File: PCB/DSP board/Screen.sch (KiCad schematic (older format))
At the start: 20 parts, among them J701 Conn_01x40_Female, J702 Conn_01x06_Female

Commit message: Schematic updates + PCB placement
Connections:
- net I2C1_SCL: now also RN709.2 (R2.1); no longer RN709.3 (R3.1)
- net I2C1_SDA: now also RN709.3 (R3.1); no longer RN709.4 (R4.1)
- net LCD_B0: now also RN704.1 (R1.1); no longer RN704.4 (R4.1)
- net LCD_B2: now also RN704.2 (R2.1); no longer RN704.3 (R3.1)
- net LCD_B4: now also RN704.3 (R3.1); no longer RN704.2 (R2.1)
- net LCD_B6: now also RN704.4 (R4.1); no longer RN704.1 (R1.1)
- net LCD_G0: now also RN706.1 (R1.1); no longer RN706.4 (R4.1)
- net LCD_G2: now also RN706.2 (R2.1); no longer RN706.3 (R3.1)
- net LCD_G4: now also RN706.3 (R3.1); no longer RN706.2 (R2.1)
- net LCD_G6: now also RN706.4 (R4.1); no longer RN706.1 (R1.1)
- net LCD_R0: now also RN708.1 (R1.1); no longer RN708.4 (R4.1)
- net LCD_R2: now also RN708.2 (R2.1); no longer RN708.3 (R3.1)
- net LCD_R4: now also RN708.3 (R3.1); no longer RN708.2 (R2.1)
- net LCD_R6: now also RN708.4 (R4.1); no longer RN708.1 (R1.1)
- net LCD_VSYNC: now also RN702.1 (R1.1); no longer RN702.4 (R4.1)
- net TFT_B0: now also RN704.8 (R1.2); no longer RN704.5 (R4.2)
- net TFT_B2: now also RN704.7 (R2.2); no longer RN704.6 (R3.2)
- net TFT_B4: now also RN704.6 (R3.2); no longer RN704.7 (R2.2)
- net TFT_B6: now also RN704.5 (R4.2); no longer RN704.8 (R1.2)
- net TFT_G0: now also RN706.8 (R1.2); no longer RN706.5 (R4.2)
- net TFT_G2: now also RN706.7 (R2.2); no longer RN706.6 (R3.2)
- net TFT_G4: now also RN706.6 (R3.2); no longer RN706.7 (R2.2)
- net TFT_G6: now also RN706.5 (R4.2); no longer RN706.8 (R1.2)
- net TFT_NINT: now also RN709.8 (R1.2); no longer RN709.7 (R2.2)
- net TFT_NRESET: now also RN709.5 (R4.2); no longer RN709.8 (R1.2)
- net TFT_R0: now also RN708.8 (R1.2); no longer RN708.5 (R4.2)
- net TFT_R2: now also RN708.7 (R2.2); no longer RN708.6 (R3.2)
- net TFT_R4: now also RN708.6 (R3.2); no longer RN708.7 (R2.2)
- net TFT_R6: now also RN708.5 (R4.2); no longer RN708.8 (R1.2)
- net TFT_SCL: now also RN709.7 (R2.2); no longer RN709.5 (R4.2)
- net TFT_VSD: now also RN702.8 (R1.2); no longer RN702.5 (R4.2)
- net TOUCH_NINT: now also RN709.1 (R1.1); no longer RN709.2 (R2.1)
- net TOUCH_NRESET: now also RN709.4 (R4.1); no longer RN709.1 (R1.1)
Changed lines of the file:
@@
 	0    1    1    0
 $EndComp
+Text GLabel 1575 7100 0    60   Input ~ 0
+LCD_R0
+Text GLabel 1575 7200 0    60   Input ~ 0
+LCD_R2
+Text GLabel 1575 7300 0    60   Input ~ 0
+LCD_R4
 Text GLabel 1575 7400 0    60   Input ~ 0
-LCD_R0
-Text GLabel 1575 7300 0    60   Input ~ 0
-LCD_R2
-Text GLabel 1575 7200 0    60   Input ~ 0
-LCD_R4
-Text GLabel 1575 7100 0    60   Input ~ 0
 LCD_R6
 Text GLabel 1575 6625 0    60   Input ~ 0
@@
 Text GLabel 1575 6325 0    60   Input ~ 0
 LCD_R7
+Text GLabel 1575 5550 0    60   Input ~ 0
+LCD_G0
+Text GLabel 1575 5650 0    60   Input ~ 0
+LCD_G2
+Text GLabel 1575 5750 0    60   Input ~ 0
+LCD_G4
 Text GLabel 1575 5850 0    60   Input ~ 0
-LCD_G0
-Text GLabel 1575 5750 0    60   Input ~ 0
-LCD_G2
-Text GLabel 1575 5650 0    60   Input ~ 0
-LCD_G4
-Text GLabel 1575 5550 0    60   Input ~ 0
 LCD_G6
 Text GLabel 1575 5050 0    60   Input ~ 0
@@
 Text GLabel 1575 4750 0    60   Input ~ 0
 LCD_G7
+Text GLabel 1575 3975 0    60   Input ~ 0
+LCD_B0
+Text GLabel 1575 4075 0    60   Input ~ 0
+LCD_B2
+Text GLabel 1575 4175 0    60   Input ~ 0
+LCD_B4
 Text GLabel 1575 4275 0    60   Input ~ 0
-LCD_B0
-Text GLabel 1575 4175 0    60   Input ~ 0
-LCD_B2
-Text GLabel 1575 4075 0    60   Input ~ 0
-LCD_B4
-Text GLabel 1575 3975 0    60   Input ~ 0
 LCD_B6
 Text GLabel 1575 3500 0    60   Input ~ 0
@@
 	0    1    1    0
 $EndComp
-Text GLabel 1575 2725 0    60   Input ~ 0
+Text GLabel 1575 2425 0    60   Input ~ 0
 LCD_VSYNC
 Text GLabel 1550 1975 0    60   Input ~ 0
@@
 	1550 1975 1700 1975
 Wire Wire Line
-	1575 2725 1700 2725
+	1575 2425 1700 2425
 Wire Wire Line
 	1575 3200 1700 3200
@@
 Text GLabel 2200 1975 2    60   Output ~ 0
 TFT_CLKIN
-Text GLabel 2200 2725 2    60   Output ~ 0
+Text GLabel 2200 2425 2    60   Output ~ 0
 TFT_VSD
 Text GLabel 2200 3200 2    60   Output ~ 0
@@
 Text GLabel 2200 3500 2    60   Output ~ 0
 TFT_B1
+Text GLabel 2200 4275 2    60   Output ~ 0
+TFT_B6
+Text GLabel 2200 4175 2    60   Output ~ 0
+TFT_B4
+Text GLabel 2200 4075 2    60   Output ~ 0
+TFT_B2
 Text GLabel 2200 3975 2    60   Output ~ 0
-TFT_B6
-Text GLabel 2200 4075 2    60   Output ~ 0
-TFT_B4
-Text GLabel 2200 4175 2    60   Output ~ 0
-TFT_B2
-Text GLabel 2200 4275 2    60   Output ~ 0
 TFT_B0
 Text GLabel 2200 4750 2    60   Output ~ 0
@@
 Text GLabel 2200 5050 2    60   Output ~ 0
 TFT_G1
+Text GLabel 2200 5850 2    60   Output ~ 0
+TFT_G6
+Text GLabel 2200 5750 2    60   Output ~ 0
+TFT_G4
+Text GLabel 2200 5650 2    60   Output ~ 0
+TFT_G2
 Text GLabel 2200 5550 2    60   Output ~ 0
-TFT_G6
-Text GLabel 2200 5650 2    60   Output ~ 0
-TFT_G4
-Text GLabel 2200 5750 2    60   Output ~ 0
-TFT_G2
-Text GLabel 2200 5850 2    60   Output ~ 0
 TFT_G0
 Text GLabel 2200 6325 2    60   Output ~ 0
@@
 Text GLabel 2200 6625 2    60   Output ~ 0
 TFT_R1
+Text GLabel 2200 7400 2    60   Output ~ 0
+TFT_R6
+Text GLabel 2200 7300 2    60   Output ~ 0
+TFT_R4
+Text GLabel 2200 7200 2    60   Output ~ 0
+TFT_R2
 Text GLabel 2200 7100 2    60   Output ~ 0
-TFT_R6
-Text GLabel 2200 7200 2    60   Output ~ 0
-TFT_R4
-Text GLabel 2200 7300 2    60   Output ~ 0
-TFT_R2
-Text GLabel 2200 7400 2    60   Output ~ 0
 TFT_R0
 Wire Wire Line
@@
 	2100 1975 2200 1975
 Wire Wire Line
-	2100 2725 2200 2725
+	2100 2425 2200 2425
 Wire Wire Line
 	2100 3200 2200 3200
@@
 	0    1    1    0
 $EndComp
-Text GLabel 8100 1650 2    60   Output ~ 0
+Text GLabel 8100 1950 2    60   Output ~ 0
 TFT_NRESET
-Text GLabel 8100 1750 2    60   Input ~ 0
+Text GLabel 8100 1650 2    60   Input ~ 0
 TFT_NINT
 Text GLabel 8100 1850 2    60   BiDi ~ 0
 TFT_SDA
-Text GLabel 8100 1950 2    60   BiDi ~ 0
+Text GLabel 8100 1750 2    60   BiDi ~ 0
 TFT_SCL
 Wire Wire Line
@@
 Wire Wire Line
 	8000 1650 8100 1650
+Text GLabel 7500 1750 0    60   BiDi ~ 0
+I2C1_SCL
 Text GLabel 7500 1850 0    60   BiDi ~ 0
-I2C1_SCL
-Text GLabel 7500 1950 0    60   BiDi ~ 0
 I2C1_SDA
-Text GLabel 7500 1650 0    60   Input ~ 0
+Text GLabel 7500 1950 0    60   Input ~ 0
 TOUCH_NRESET
-Text GLabel 7500 1750 0    60   Output ~ 0
+Text GLabel 7500 1650 0    60   Output ~ 0
 TOUCH_NINT
 Wire Wire Line
@@
 NoConn ~ 1700 1675
 NoConn ~ 2100 1675
-NoConn ~ 1700 2425
-NoConn ~ 2100 2425
-NoConn ~ 2100 2525
-NoConn ~ 2100 2625
-NoConn ~ 1700 2625
-NoConn ~ 1700 2525
 NoConn ~ 3900 2025
 NoConn ~ 3900 3350
 NoConn ~ 3900 3450
 NoConn ~ 3900 3550
+NoConn ~ 1700 2525
+NoConn ~ 1700 2625
+NoConn ~ 1700 2725
+NoConn ~ 2100 2525
+NoConn ~ 2100 2625
+NoConn ~ 2100 2725
 $EndSCHEMATC

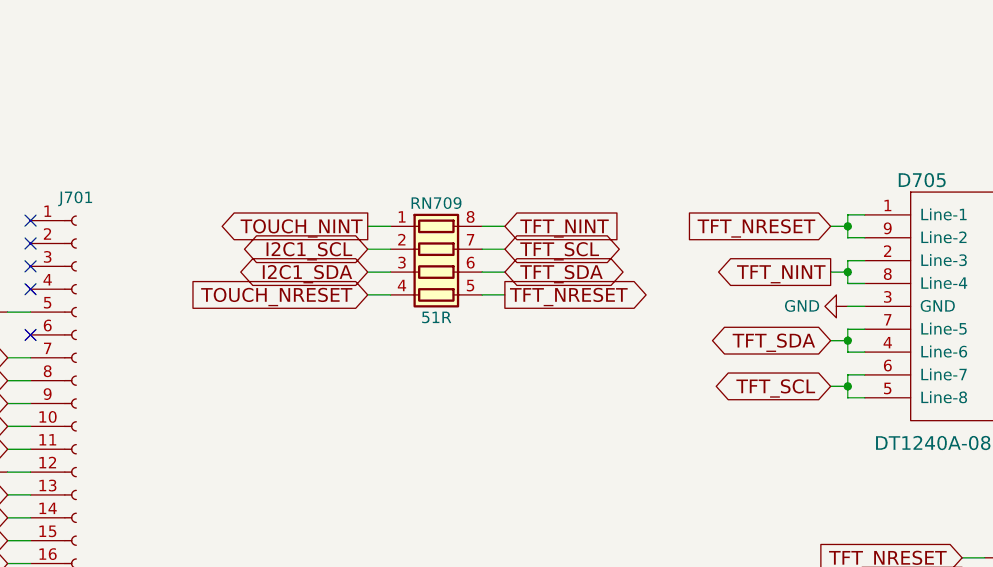
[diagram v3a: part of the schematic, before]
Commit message: Component Placement - RN
All components placed except for RAM Resistor Networks
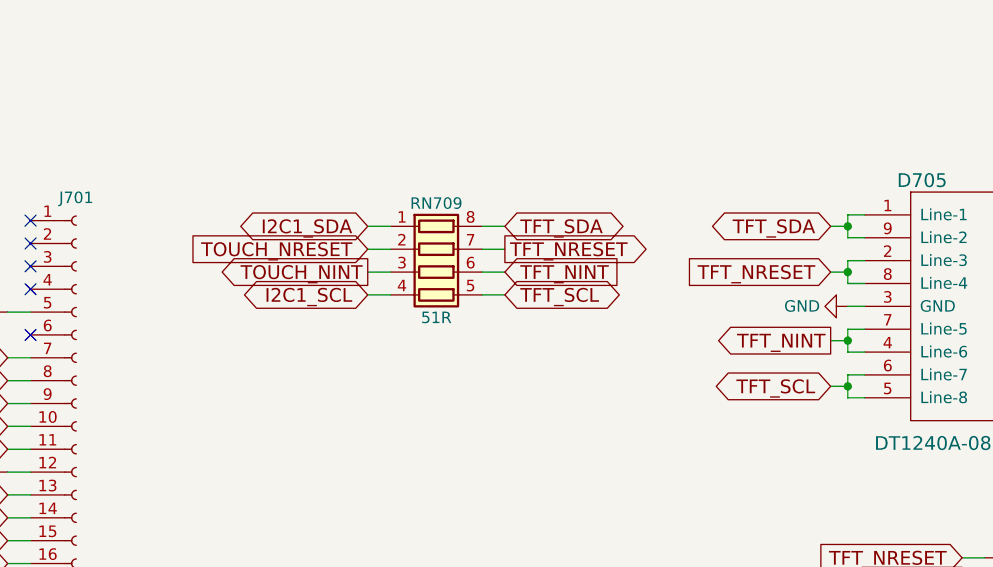
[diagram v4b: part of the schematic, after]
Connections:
- net I2C1_SCL: now also RN709.4 (R4.1); no longer RN709.2 (R2.1)
- net I2C1_SDA: now also RN709.1 (R1.1); no longer RN709.3 (R3.1)
- net TFT_NINT: now also D705.4 (Line-6), D705.7 (Line-5), RN709.6 (R3.2); no longer D705.2 (Line-3), D705.8 (Line-4), RN709.8 (R1.2)
- net TFT_NRESET: now also D705.2 (Line-3), D705.8 (Line-4), RN709.7 (R2.2); no longer D705.1 (Line-1), D705.9 (Line-2), RN709.5 (R4.2)
- net TFT_SCL: now also RN709.5 (R4.2); no longer RN709.7 (R2.2)
- net TFT_SDA: now also D705.1 (Line-1), D705.9 (Line-2), RN709.8 (R1.2); no longer D705.4 (Line-6), D705.7 (Line-5), RN709.6 (R3.2)
- net TOUCH_NINT: now also RN709.3 (R3.1); no longer RN709.1 (R1.1)
- net TOUCH_NRESET: now also RN709.2 (R2.1); no longer RN709.4 (R4.1)
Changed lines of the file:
@@
 Wire Wire Line
 	10100 3100 10200 3100
-Text GLabel 9525 1650 0    60   Input ~ 0
+Text GLabel 9525 1850 0    60   Input ~ 0
 TFT_NRESET
-Text GLabel 9525 1850 0    60   Output ~ 0
+Text GLabel 9525 2150 0    60   Output ~ 0
 TFT_NINT
-Text GLabel 9525 2150 0    60   BiDi ~ 0
+Text GLabel 9525 1650 0    60   BiDi ~ 0
 TFT_SDA
 Text GLabel 9525 2350 0    60   BiDi ~ 0
@@
 	0    1    1    0
 $EndComp
-Text GLabel 8100 1950 2    60   Output ~ 0
+Text GLabel 8100 1750 2    60   Output ~ 0
 TFT_NRESET
-Text GLabel 8100 1650 2    60   Input ~ 0
+Text GLabel 8100 1850 2    60   Input ~ 0
 TFT_NINT
-Text GLabel 8100 1850 2    60   BiDi ~ 0
+Text GLabel 8100 1650 2    60   BiDi ~ 0
 TFT_SDA
-Text GLabel 8100 1750 2    60   BiDi ~ 0
+Text GLabel 8100 1950 2    60   BiDi ~ 0
 TFT_SCL
 Wire Wire Line
@@
 Wire Wire Line
 	8000 1650 8100 1650
-Text GLabel 7500 1750 0    60   BiDi ~ 0
+Text GLabel 7500 1950 0    60   BiDi ~ 0
 I2C1_SCL
-Text GLabel 7500 1850 0    60   BiDi ~ 0
+Text GLabel 7500 1650 0    60   BiDi ~ 0
 I2C1_SDA
-Text GLabel 7500 1950 0    60   Input ~ 0
+Text GLabel 7500 1750 0    60   Input ~ 0
 TOUCH_NRESET
-Text GLabel 7500 1650 0    60   Output ~ 0
+Text GLabel 7500 1850 0    60   Output ~ 0
 TOUCH_NINT
 Wire Wire Line

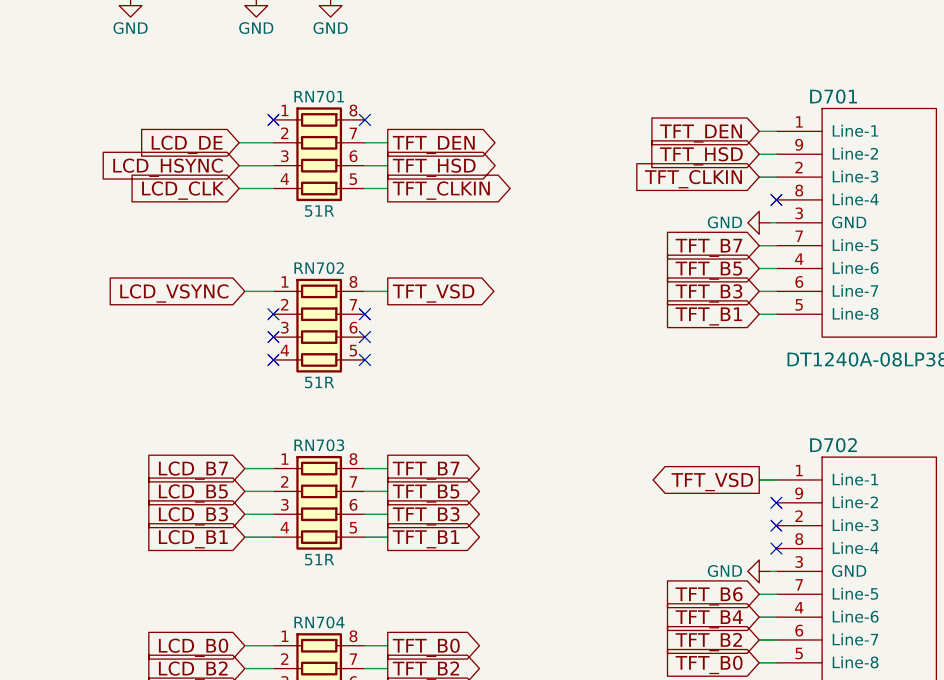
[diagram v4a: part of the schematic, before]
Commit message: RAM Routing - Data
All RAM routing & matching done, supply still needs to be done
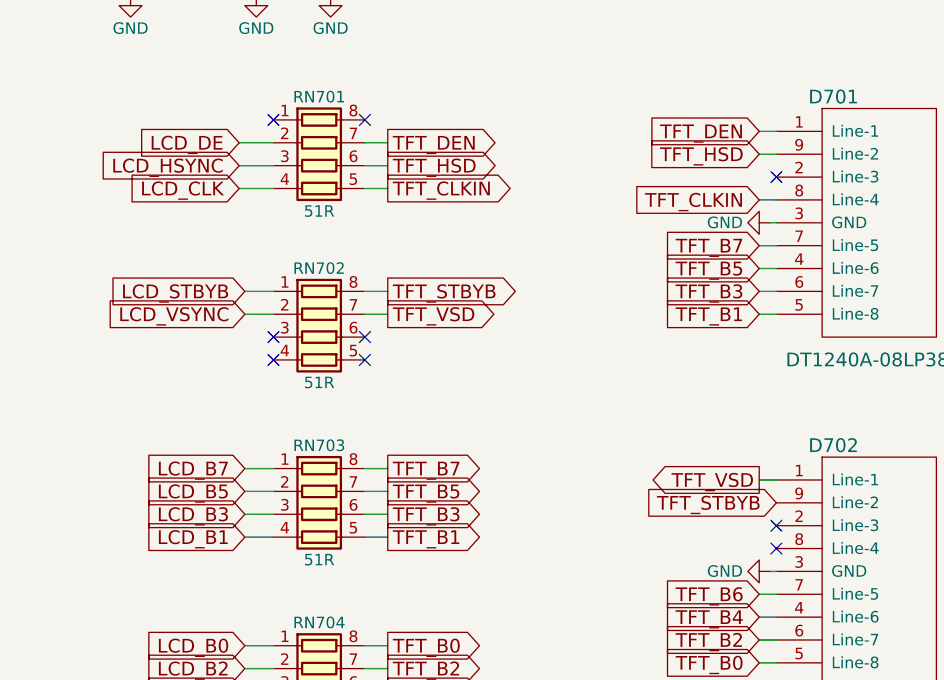
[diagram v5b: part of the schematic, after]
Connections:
- net LCD_VSYNC: now also RN702.2 (R2.1); no longer RN702.1 (R1.1)
- net TFT_CLKIN: now also D701.8 (Line-4); no longer D701.2 (Line-3)
- net TFT_STBYB: now also D702.9 (Line-2), RN702.8 (R1.2)
- net TFT_VSD: now also RN702.7 (R2.2); no longer RN702.8 (R1.2)
- new net LCD_STBYB: RN702.1 (R1.1)
- no-connect marks 17 -> 14
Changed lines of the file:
@@
 	0    1    1    0
 $EndComp
-Text GLabel 1575 2425 0    60   Input ~ 0
+Text GLabel 1575 2525 0    60   Input ~ 0
 LCD_VSYNC
 Text GLabel 1550 1975 0    60   Input ~ 0
@@
 Text GLabel 2200 1975 2    60   Output ~ 0
 TFT_CLKIN
-Text GLabel 2200 2425 2    60   Output ~ 0
+Text GLabel 2200 2525 2    60   Output ~ 0
 TFT_VSD
 Text GLabel 2200 3200 2    60   Output ~ 0
@@
 Text GLabel 3825 1825 0    60   Input ~ 0
 TFT_HSD
-Text GLabel 3825 1925 0    60   Input ~ 0
+Text GLabel 3825 2025 0    60   Input ~ 0
 TFT_CLKIN
 Text GLabel 3825 2225 0    60   Input ~ 0
@@
 	3825 1825 3900 1825
 Wire Wire Line
-	3825 1925 3900 1925
+	3825 2025 3900 2025
 Wire Wire Line
 	3825 2225 3900 2225
@@
 NoConn ~ 1700 1675
 NoConn ~ 2100 1675
-NoConn ~ 3900 2025
-NoConn ~ 3900 3350
 NoConn ~ 3900 3450
 NoConn ~ 3900 3550
-NoConn ~ 1700 2525
 NoConn ~ 1700 2625
 NoConn ~ 1700 2725
-NoConn ~ 2100 2525
 NoConn ~ 2100 2625
 NoConn ~ 2100 2725
+NoConn ~ 3900 1925
+Text GLabel 1575 2425 0    60   Input ~ 0
+LCD_STBYB
+Text GLabel 2200 2425 2    60   Output ~ 0
+TFT_STBYB
+Wire Wire Line
+	1575 2525 1700 2525
+Wire Wire Line
+	2100 2525 2200 2525
+Text GLabel 3900 3350 0    60   Input ~ 0
+TFT_STBYB
 $EndSCHEMATC
